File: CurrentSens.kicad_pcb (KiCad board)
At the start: 2 copper layers, 53 x 80 mm, 25 parts, among them J101 USB_C_Receptacle_USB2.0, J102 Conn_01x01, J103 USB_C_Receptacle_USB2.0, J104 Conn_01x01, J105 Conn_Coaxial, J106 Conn_01x04

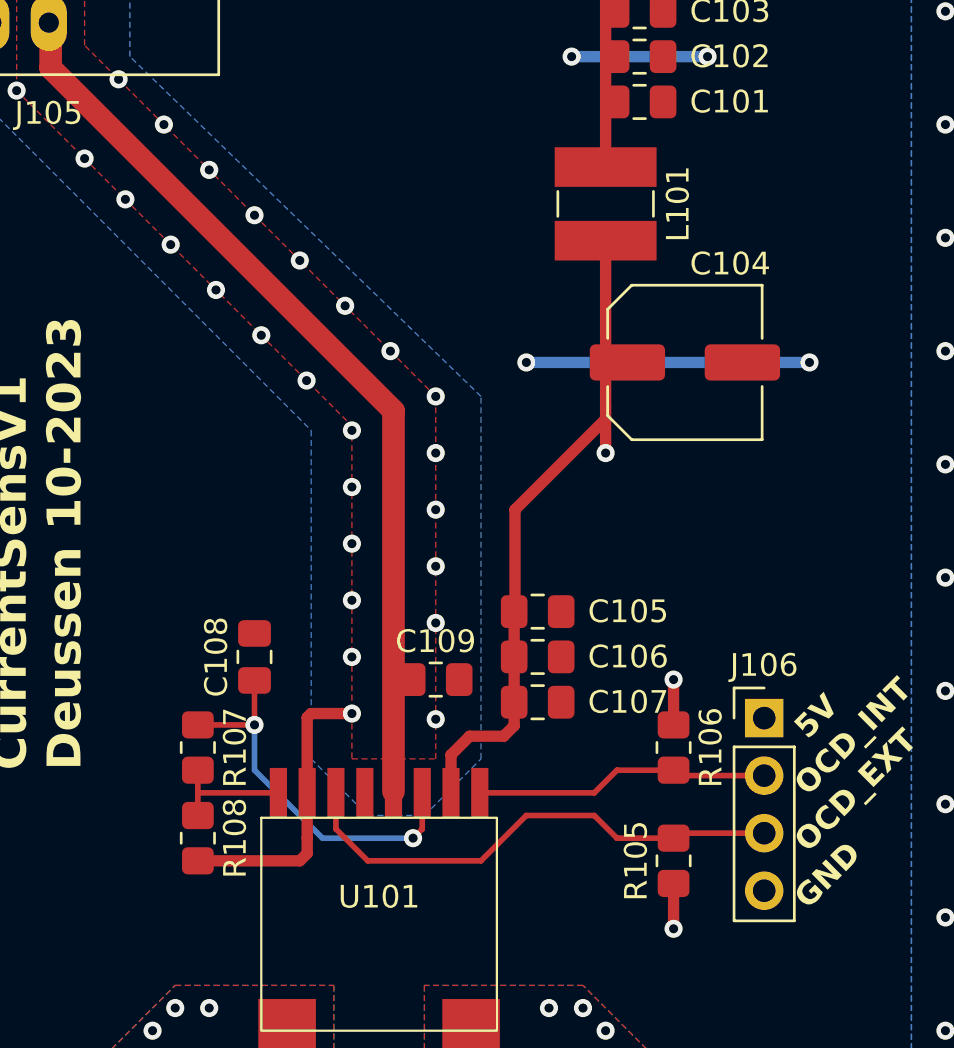
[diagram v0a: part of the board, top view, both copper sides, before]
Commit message: Some fixes for first production run at aisler - change inductor - add 3D data - fix references in silkscreen
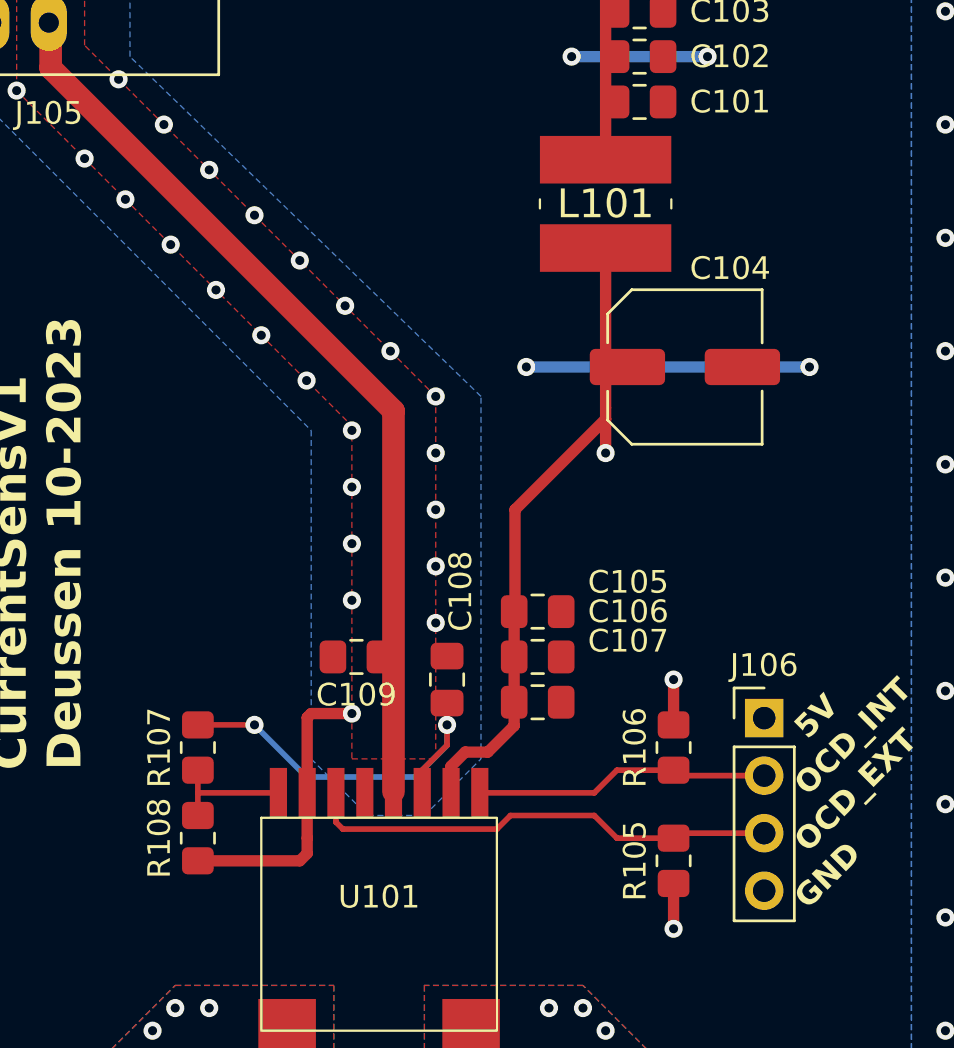
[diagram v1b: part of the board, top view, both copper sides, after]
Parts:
- L101: footprint Inductor_SMD:L_Ferrocore_DLG-0403 -> CurrentSens:SDR0604330KL
- moved C108 8.56 mm to (139.5, 92.0)
- moved C109 3.64 mm to (135.5, 91.0), turned to 180 degrees
- moved C104 0.20 mm to (150.0, 78.2)
- turned L101 to 180 degrees
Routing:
- net /OCD_EXT: track 22.4 -> 21.1 mm
- net Net-(U101-Uref): track 16.9 -> 17.8 mm
- net +5V: track 33.6 -> 33.0 mm
- net GND: vias 62 -> 60

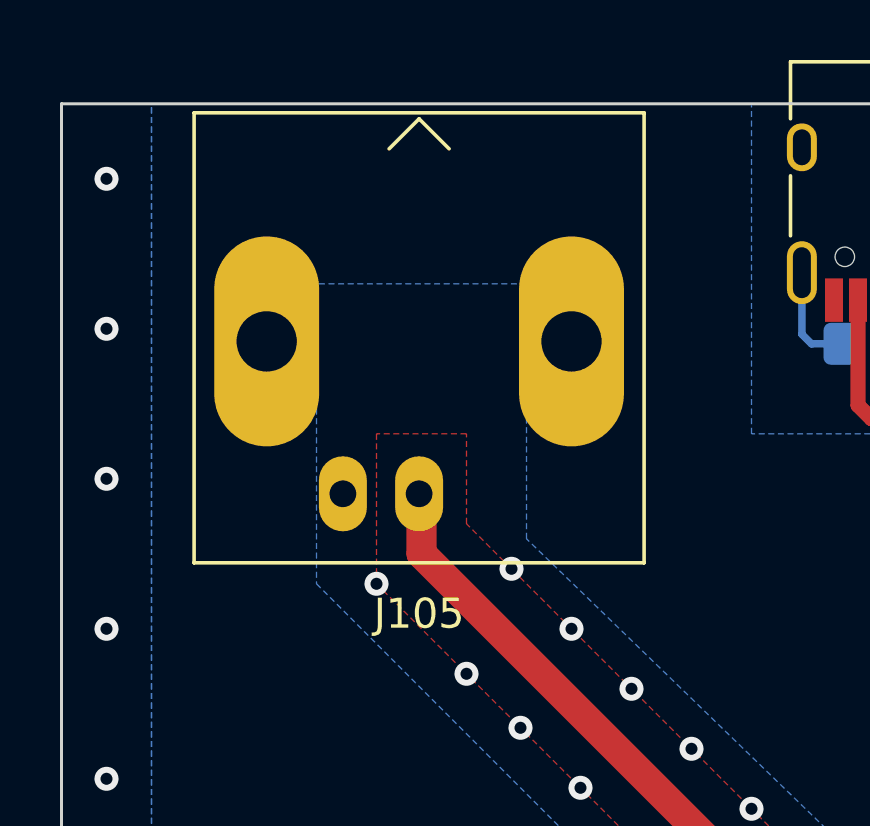
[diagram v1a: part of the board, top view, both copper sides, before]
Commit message: Adjust position of BNC jack
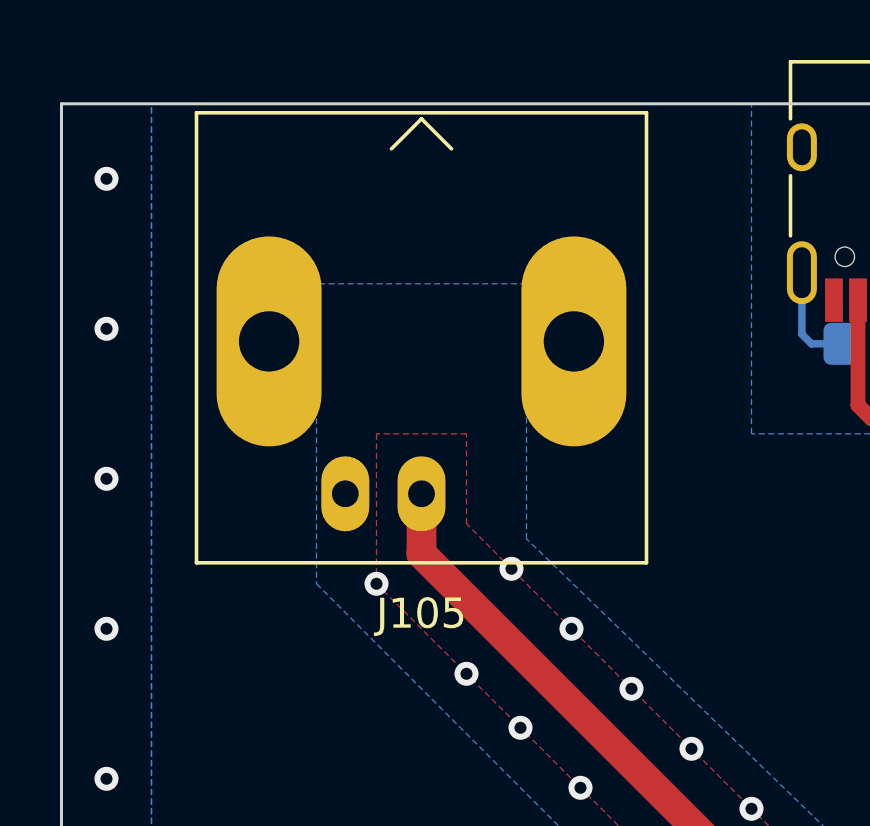
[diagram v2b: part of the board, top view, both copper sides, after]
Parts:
- moved J105 0.08 mm to (122.0, 63.0)
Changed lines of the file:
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@@
   )
   (footprint "Connector_Coaxial:BNC_Amphenol_B6252HB-NPP3G-50_Horizontal" (layer "F.Cu")
-    (at 121.92 63)
+    (at 122 63)
     (descr "http://www.farnell.com/datasheets/612848.pdf")
     (tags "BNC Amphenol Horizontal")
@@
   (segment (start 152 60.5) (end 156 60.5) (width 0.5) (layer "F.Cu") (net 18))
   (segment (start 137.135 80.135) (end 137.135 96.95) (width 1) (layer "F.Cu") (net 19))
-  (segment (start 122 63.08) (end 122 65) (width 1) (layer "F.Cu") (net 19))
-  (segment (start 121.92 63) (end 122 63.08) (width 1) (layer "F.Cu") (net 19))
+  (segment (start 122 65) (end 122 63) (width 1) (layer "F.Cu") (net 19))
   (segment (start 122 65) (end 137.135 80.135) (width 1) (layer "F.Cu") (net 19))
   (segment (start 153 59.2) (end 152.25 58.45) (width 0.25) (layer "F.Cu") (net 23))
